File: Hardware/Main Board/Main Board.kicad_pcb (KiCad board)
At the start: 2 copper layers, 100 x 100 mm, 63 parts, among them J1 USB_C_Receptacle_USB2.0, J10 Conn_01x02, J2 Conn_02x20_Odd_Even, J3 PWR_SW, J4 Conn_02x20_Odd_Even, J5 Conn_02x02_Odd_Even, J6 RESET_SW, J7 CLOCK_ENBL_SW, J8 Conn_02x05_Odd_Even, J9 Conn_02x01, Q1 Q_NPN_BEC, SW1 Reset, U1 74HC00, U2 74HC00, U3 74HC00, U4 LM555xM, U5 65C02, U6 AS6C62256, U7 AT28C256, X1 OCXO-14

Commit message: Final serial cards
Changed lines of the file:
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@@
 			)
 		)
-		(property "Footprint" ""
+		(property "Footprint" "Symbol:OSHW-Logo2_7.3x6mm_SilkScreen"
 			(at 0 0 0)
 			(unlocked yes)
@@
 		(tags "resistor")
 		(property "Reference" "R15"
-			(at 0 -1.8 270)
+			(at 0 -1.8 -90)
 			(layer "F.SilkS")
 			(effects
@@
 		)
 		(property "Value" "1k"
-			(at 0 1.65 270)
+			(at 0 1.65 -90)
 			(layer "F.Fab")
 			(hide yes)
@@
 		)
 		(fp_text user "${REFERENCE}"
-			(at 0 0 270)
+			(at 0 0 -90)
 			(layer "F.Fab")
 			(effects
@@
 		(tags "resistor")
 		(property "Reference" "R12"
-			(at 0 -1.9 270)
+			(at 0 -1.9 -90)
 			(layer "F.SilkS")
 			(effects
@@
 		)
 		(property "Value" "1k"
-			(at 0 1.65 270)
+			(at 0 1.65 -90)
 			(layer "F.Fab")
 			(hide yes)
@@
 		)
 		(fp_text user "${REFERENCE}"
-			(at 0 0 270)
+			(at 0 0 -90)
 			(layer "F.Fab")
 			(effects
@@
 	)
 	(gr_text "JLCJLCJLCJLC"
-		(at 166.2 89 90)
+		(at 118.075 70.25 0)
 		(layer "F.SilkS")
 		(effects

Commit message: Production updates
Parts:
- moved REF** 84.1 mm to (156.6, 60.8)
- moved R10 2.49 mm to (169.1, 132.8), turned to 90 degrees
- moved R3 0.90 mm to (155.7, 65.5)
- moved C1 0.90 mm to (140.4, 65.4)
- moved C2 0.90 mm to (155.7, 70.9)
- moved Q1 0.90 mm to (154.9, 76.4)
- moved R2 0.90 mm to (140.4, 71.0)
- moved R4 0.90 mm to (146.0, 72.5)
- moved R8 0.90 mm to (150.2, 72.5)
- moved U1 0.90 mm to (148.1, 66.5)
- moved C5 0.90 mm to (150.1, 62.0)
- moved R9 0.35 mm to (132.8, 100.7)
- moved R12 0.27 mm to (158.9, 119.1)
- turned R1 to -90 degrees
- renumbered C5 to C1, C2 to C10, C4 to C11, C7 to C2, C10 to C3, C11 to C4, C1 to C5, C3 to C6, C6 to C7, J3 to J1, J4 to J10, J9 to J2, J1 to J3, J6 to J4, J7 to J6, J10 to J7, J2 to J9, JP5 to JP1, JP1 to JP2, JP2 to JP3, JP3 to JP4, JP6 to JP5, JP4 to JP6, R9 to R1, R11 to R10, R12 to R11, R13 to R12, R14 to R13, R15 to R14, R5 to R2, R6 to R3, R8 to R4, R1 to R5, R2 to R6, R4 to R7, R7 to R8, R3 to R9, U4 to U1, U6 to U2, U7 to U3, U2 to U4, U3 to U5, U5 to U6, U1 to U7
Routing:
- net VCC: track 144.6 -> 402.1 mm, vias 0 -> 13
- net EXP1: track 15.8 -> 174.5 mm, vias 0 -> 3
- net EXP0: track 21.9 -> 173.7 mm, vias 0 -> 4
- net D2: track 18.7 -> 163.2 mm, vias 0 -> 4
- net D1: track 18.9 -> 159.2 mm, vias 0 -> 4
- net A3: track 21.9 -> 161.0 mm, vias 0 -> 4
- net A4: track 21.9 -> 159.7 mm, vias 0 -> 7
- net A2: track 21.9 -> 159.4 mm, vias 0 -> 7
- net D0: track 18.1 -> 154.2 mm, vias 0 -> 4
- net A13: track 21.9 -> 152.7 mm, vias 0 -> 6
- net A1: track 21.9 -> 151.9 mm, vias 0 -> 7
- net D5: track 18.7 -> 147.6 mm, vias 0 -> 5
- net A11: track 21.9 -> 148.1 mm, vias 0 -> 5
- net A5: track 21.9 -> 148.1 mm, vias 0 -> 4
- net D7: track 18.9 -> 144.6 mm, vias 0 -> 3
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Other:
- board text added: "6502"
- board text added: "EXP0 | VPB"
- board text added: "EXP1 | MLB"
- board text added: "EXP2 | SOB"
- board text added: "EXP3 | PHI1O"
- board text added: "EXP3 | PHI2O"
- board text added: "IC2 RAM"
- board text added: "RAM"
- board text added: "ROM"
- board text added: "~{HI ROM DISABLE}"

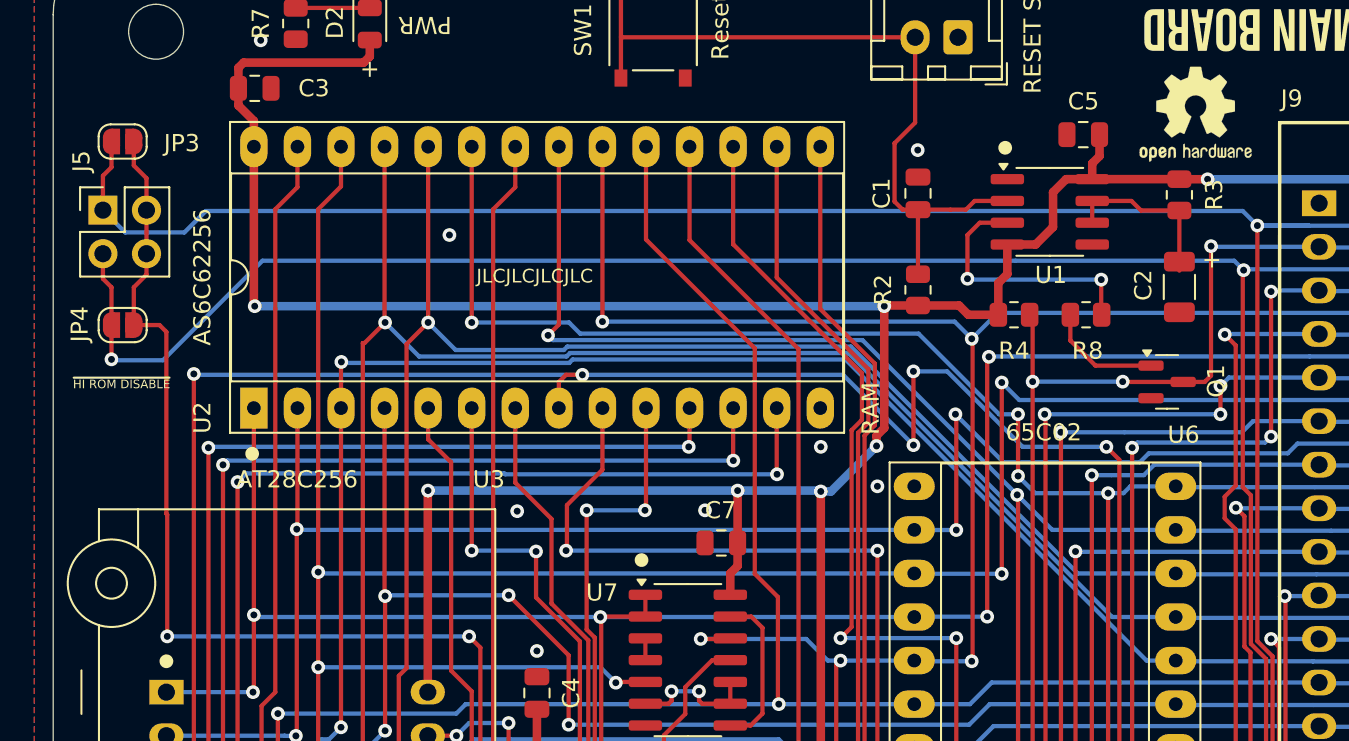
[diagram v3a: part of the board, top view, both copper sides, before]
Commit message: Add Input Board and rework Debugger
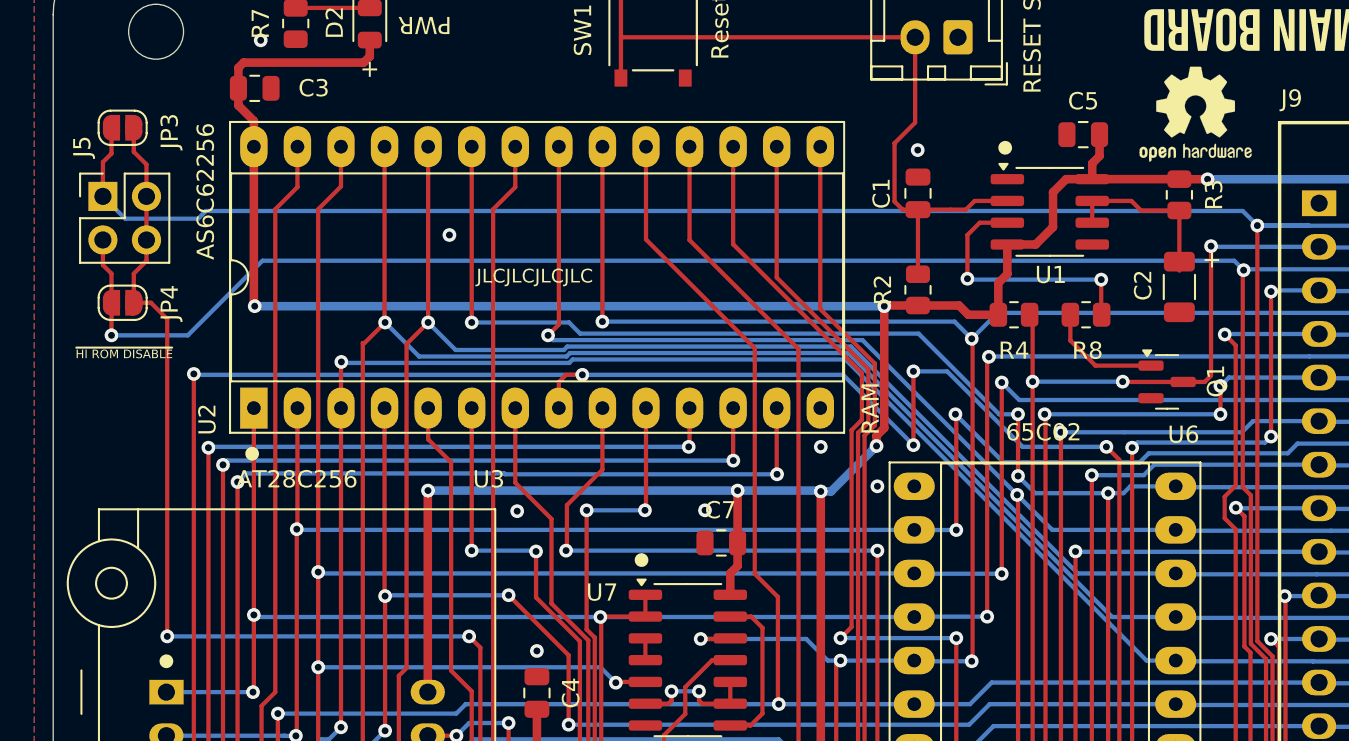
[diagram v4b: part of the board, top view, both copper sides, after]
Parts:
- moved JP4 1.30 mm to (94.0, 71.8)
- moved J5 0.80 mm to (92.9, 65.6)
- moved JP3 0.80 mm to (94.0, 61.6)
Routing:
- net EXP0: track 173.7 -> 172.5 mm
- net HRDB: track 79.5 -> 80.0 mm
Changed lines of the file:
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@@
 	(title_block
 		(title "6502 Main Board")
-		(date "2024-06-08")
+		(date "2024-06-17")
 		(rev "1.0")
 		(company "A.C. Wright Design")
@@
 	(footprint "Jumper:SolderJumper-2_P1.3mm_Open_RoundedPad1.0x1.5mm"
 		(layer "F.Cu")
-		(at 94.05 73.1)
+		(at 94.05 71.8)
 		(descr "SMD Solder Jumper, 1x1.5mm, rounded Pads, 0.3mm gap, open")
 		(tags "solder jumper open")
 		(property "Reference" "JP4"
-			(at -2.5 -0.05 90)
+			(at 2.75 0 90)
 			(layer "F.SilkS")
 			(effects
@@
 	(footprint "Jumper:SolderJumper-2_P1.3mm_Open_RoundedPad1.0x1.5mm"
 		(layer "F.Cu")
-		(at 94.05 62.4)
+		(at 94.05 61.6)
 		(descr "SMD Solder Jumper, 1x1.5mm, rounded Pads, 0.3mm gap, open")
 		(tags "solder jumper open")
 		(property "Reference" "JP3"
-			(at 3.45 0.1 0)
+			(at 2.75 0.2 90)
 			(layer "F.SilkS")
 			(effects
@@
 		(tags "THT DIP DIL PDIP 2.54mm 15.24mm 600mil Socket LongPads")
 		(property "Reference" "U2"
-			(at -0.56 -3 -90)
+			(at -0.66 -2.7 -90)
 			(layer "F.SilkS")
 			(effects
@@
 		)
 		(property "Value" "AS6C62256"
-			(at 7.64 -3 -90)
+			(at 12.64 -2.8 -90)
 			(layer "F.SilkS")
 			(effects
@@
 	(footprint "Connector_PinHeader_2.54mm:PinHeader_2x02_P2.54mm_Vertical"
 		(layer "F.Cu")
-		(at 92.9 66.4)
+		(at 92.9 65.6)
 		(descr "Through hole straight pin header, 2x02, 2.54mm pitch, double rows")
 		(tags "Through hole pin header THT 2x02 2.54mm double row")
 		(property "Reference" "J5"
-			(at -1.25 -2.85 90)
+			(at -1.2 -2.9 90)
 			(layer "F.SilkS")
 			(effects
@@
 	)
 	(gr_text "~{HI ROM DISABLE}"
-		(at 91.15 76.55 0)
+		(at 91.3 74.8 0)
 		(layer "F.SilkS")
 		(effects
@@
 	)
 	(segment
-		(start 126.1 102.75)
-		(end 124.565 102.75)
+		(start 96.65 72.75)
+		(end 96.65 91.25)
 		(width 0.25)
 		(layer "F.Cu")
@@
 	)
 	(segment
-		(start 94.7 70.9)
-		(end 94.7 73.1)
+		(start 95.44 68.14)
+		(end 95.44 69.36)
 		(width 0.25)
 		(layer "F.Cu")
@@
 	)
 	(segment
-		(start 94.7 63.8)
-		(end 95.44 64.54)
+		(start 126.1 102.75)
+		(end 124.565 102.75)
 		(width 0.25)
 		(layer "F.Cu")
@@
 	)
 	(segment
-		(start 94.7 62.4)
-		(end 94.7 63.8)
+		(start 94.7 63)
+		(end 95.44 63.74)
 		(width 0.25)
 		(layer "F.Cu")
@@
 	)
 	(segment
-		(start 94.7 73.1)
-		(end 96.2 73.1)
+		(start 94.7 61.6)
+		(end 94.7 63)
 		(width 0.25)
 		(layer "F.Cu")
@@
 	)
 	(segment
-		(start 128.335 103.435)
-		(end 127.65 102.75)
+		(start 94.7 71.8)
+		(end 95.7 71.8)
 		(width 0.25)
 		(layer "F.Cu")
@@
 	)
 	(segment
-		(start 95.44 64.54)
-		(end 95.44 66.4)
+		(start 128.335 103.435)
+		(end 127.65 102.75)
 		(width 0.25)
 		(layer "F.Cu")
@@
 	)
 	(segment
-		(start 124.45 102.715)
-		(end 124.525 102.79)
+		(start 95.44 63.74)
+		(end 95.44 65.6)
 		(width 0.25)
 		(layer "F.Cu")
@@
 	)
 	(segment
-		(start 96.65 84.15)
-		(end 96.65 91.25)
+		(start 94.7 70.1)
+		(end 94.7 71.8)
 		(width 0.25)
 		(layer "F.Cu")
@@
 	)
 	(segment
-		(start 96.2 73.1)
-		(end 96.6 73.5)
+		(start 124.45 102.715)
+		(end 124.525 102.79)
 		(width 0.25)
 		(layer "F.Cu")
@@
 	)
 	(segment
-		(start 95.44 66.4)
-		(end 95.44 68.94)
+		(start 95.44 65.6)
+		(end 95.44 68.14)
 		(width 0.25)
 		(layer "F.Cu")
@@
 	)
 	(segment
-		(start 95.44 68.94)
-		(end 95.44 70.16)
+		(start 95.44 69.36)
+		(end 94.7 70.1)
 		(width 0.25)
 		(layer "F.Cu")
@@
 	)
 	(segment
-		(start 124.565 102.75)
-		(end 124.525 102.79)
+		(start 95.7 71.8)
+		(end 96.65 72.75)
 		(width 0.25)
 		(layer "F.Cu")
@@
 	)
 	(segment
-		(start 95.44 70.16)
-		(end 94.7 70.9)
-		(width 0.25)
-		(layer "F.Cu")
-		(net 5)
-	)
-	(segment
-		(start 96.6 73.5)
-		(end 96.6 84.1)
+		(start 124.565 102.75)
+		(end 124.525 102.79)
 		(width 0.25)
 		(layer "F.Cu")
@@
 		(net 5)
 	)
-	(segment
-		(start 96.6 84.1)
-		(end 96.65 84.15)
-		(width 0.25)
-		(layer "F.Cu")
-		(net 5)
-	)
 	(via
 		(at 96.65 91.25)
@@
 	)
 	(segment
-		(start 93.4 62.4)
-		(end 93.4 63.9)
+		(start 93.4 61.6)
+		(end 93.4 63.1)
 		(width 0.25)
 		(layer "F.Cu")
@@
 	)
 	(segment
-		(start 93.4 63.9)
-		(end 92.9 64.4)
+		(start 93.4 63.1)
+		(end 92.9 63.6)
 		(width 0.25)
 		(layer "F.Cu")
@@
 	)
 	(segment
-		(start 92.9 64.4)
-		(end 92.9 66.4)
+		(start 92.9 63.6)
+		(end 92.9 65.6)
 		(width 0.25)
 		(layer "F.Cu")
@@
 	)
 	(segment
+		(start 94.2 66.9)
+		(end 92.9 65.6)
+		(width 0.25)
+		(layer "B.Cu")
+		(net 6)
+	)
+	(segment
 		(start 154.2 133.7)
 		(end 154.255 133.645)
@@
 	)
 	(segment
-		(start 160.2 67.3)
-		(end 163.19 67.3)
+		(start 98.9 66.45)
+		(end 98.45 66.9)
 		(width 0.25)
 		(layer "B.Cu")
@@
 	(segment
 		(start 160.2 67.3)
-		(end 159.35 66.45)
+		(end 163.19 67.3)
 		(width 0.25)
 		(layer "B.Cu")
@@
 	)
 	(segment
-		(start 98.9 66.45)
-		(end 97.65 67.7)
+		(start 160.2 67.3)
+		(end 159.35 66.45)
 		(width 0.25)
 		(layer "B.Cu")
@@
 	)
 	(segment
-		(start 97.65 67.7)
-		(end 94.2 67.7)
-		(width 0.25)
-		(layer "B.Cu")
-		(net 6)
-	)
-	(segment
 		(start 163.01 67.31)
 		(end 163 67.3)
@@
 	)
 	(segment
-		(start 94.2 67.7)
-		(end 92.9 66.4)
+		(start 159.35 66.45)
+		(end 98.9 66.45)
 		(width 0.25)
 		(layer "B.Cu")
@@
 	)
 	(segment
-		(start 159.35 66.45)
-		(end 98.9 66.45)
+		(start 169.926 67.31)
+		(end 168.681 68.555)
 		(width 0.25)
 		(layer "B.Cu")
@@
 	)
 	(segment
-		(start 169.926 67.31)
-		(end 168.681 68.555)
+		(start 98.45 66.9)
+		(end 94.2 66.9)
 		(width 0.25)
 		(layer "B.Cu")
@@
 	)
 	(segment
-		(start 92.9 68.94)
-		(end 92.9 70.4)
+		(start 92.9 69.6)
+		(end 92.9 68.14)
 		(width 0.25)
 		(layer "F.Cu")
@@
 	)
 	(segment
-		(start 93.4 75.1)
-		(end 93.4 73.1)
-		(width 0.25)
-		(layer "F.Cu")
-		(net 7)
-	)
-	(segment
 		(start 160.709 130.691)
 		(end 160.709 92.568468)
@@
 	)
 	(segment
-		(start 92.9 70.4)
-		(end 93.4 70.9)
+		(start 93.4 70.1)
+		(end 92.9 69.6)
 		(width 0.25)
 		(layer "F.Cu")
@@
 	)
 	(segment
-		(start 93.4 70.9)
-		(end 93.4 73.1)
+		(start 93.4 73.7)
+		(end 93.4 70.1)
 		(width 0.25)
 		(layer "F.Cu")
@@
 	)
 	(via
-		(at 93.4 75.1)
+		(at 93.4 73.7)
 		(size 0.8)
 		(drill 0.4)
@@
 	(segment
 		(start 158.85 69.35)
-		(end 146.1 69.35)
+		(end 159.4 69.9)
 		(width 0.25)
 		(layer "B.Cu")
@@
 	(segment
 		(start 102.2 69.35)
-		(end 96.4 75.15)
+		(end 158.85 69.35)
 		(width 0.25)
 		(layer "B.Cu")
@@
 	)
 	(segment
-		(start 178.333174 69.85)
-		(end 180.34 69.85)
-		(width 0.25)
-		(layer "B.Cu")
-		(net 7)
-	)
-	(segment
-		(start 146.1 69.35)
+		(start 97.85 73.7)
 		(end 102.2 69.35)
 		(width 0.25)
@@
 	)
 	(segment
-		(start 96.4 75.15)
-		(end 93.45 75.15)
-		(width 0.25)
-		(layer "B.Cu")
-		(net 7)
-	)
-	(segment
-		(start 93.45 75.15)
-		(end 93.4 75.1)
+		(start 178.333174 69.85)
+		(end 180.34 69.85)
 		(width 0.25)
 		(layer "B.Cu")
@@
 	)
 	(segment
-		(start 159.4 69.9)
-		(end 158.85 69.35)
+		(start 93.4 73.7)
+		(end 97.85 73.7)
 		(width 0.25)
 		(layer "B.Cu")

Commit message: Revise some boards
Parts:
- J10: footprint Connector_PinHeader_2.54mm:PinHeader_2x20_P2.54mm_Vertical -> 6502 Parts:6502 Bus Connector
- moved C6 3.06 mm to (177.4, 59.8)
- moved TP3 0.90 mm to (179.6, 124.0)
- moved C11 0.80 mm to (180.3, 120.8)
- moved D1 0.80 mm to (173.2, 126.6)
- moved TP1 0.80 mm to (173.2, 120.8)
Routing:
- net VCC: track 402.1 -> 406.1 mm
- net Net-(D1-A): track 13.1 -> 12.3 mm
